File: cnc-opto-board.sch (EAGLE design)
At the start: 25 parts, among them J1 TTL, J2 FIELD, J3 POWER, Q1 P2N2222A, Q2 P2N2222A, U1 ATTINY85

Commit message: UPDATE: sized board outline to fit DIN rail mount frame and routed.
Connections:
- net +24V: now also J3-3.1; no longer J3-1.1
- net +5V: now also J3-1.1; no longer J3-2.1
- net GND: now also J3-2.1; no longer J3-3.1
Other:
- moved on the sheet: J1-1, J1-2, J1-3, J1-4, J1-5, J2-1, J2-2, J2-3, J2-4, J2-5, J2-6, J3-1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

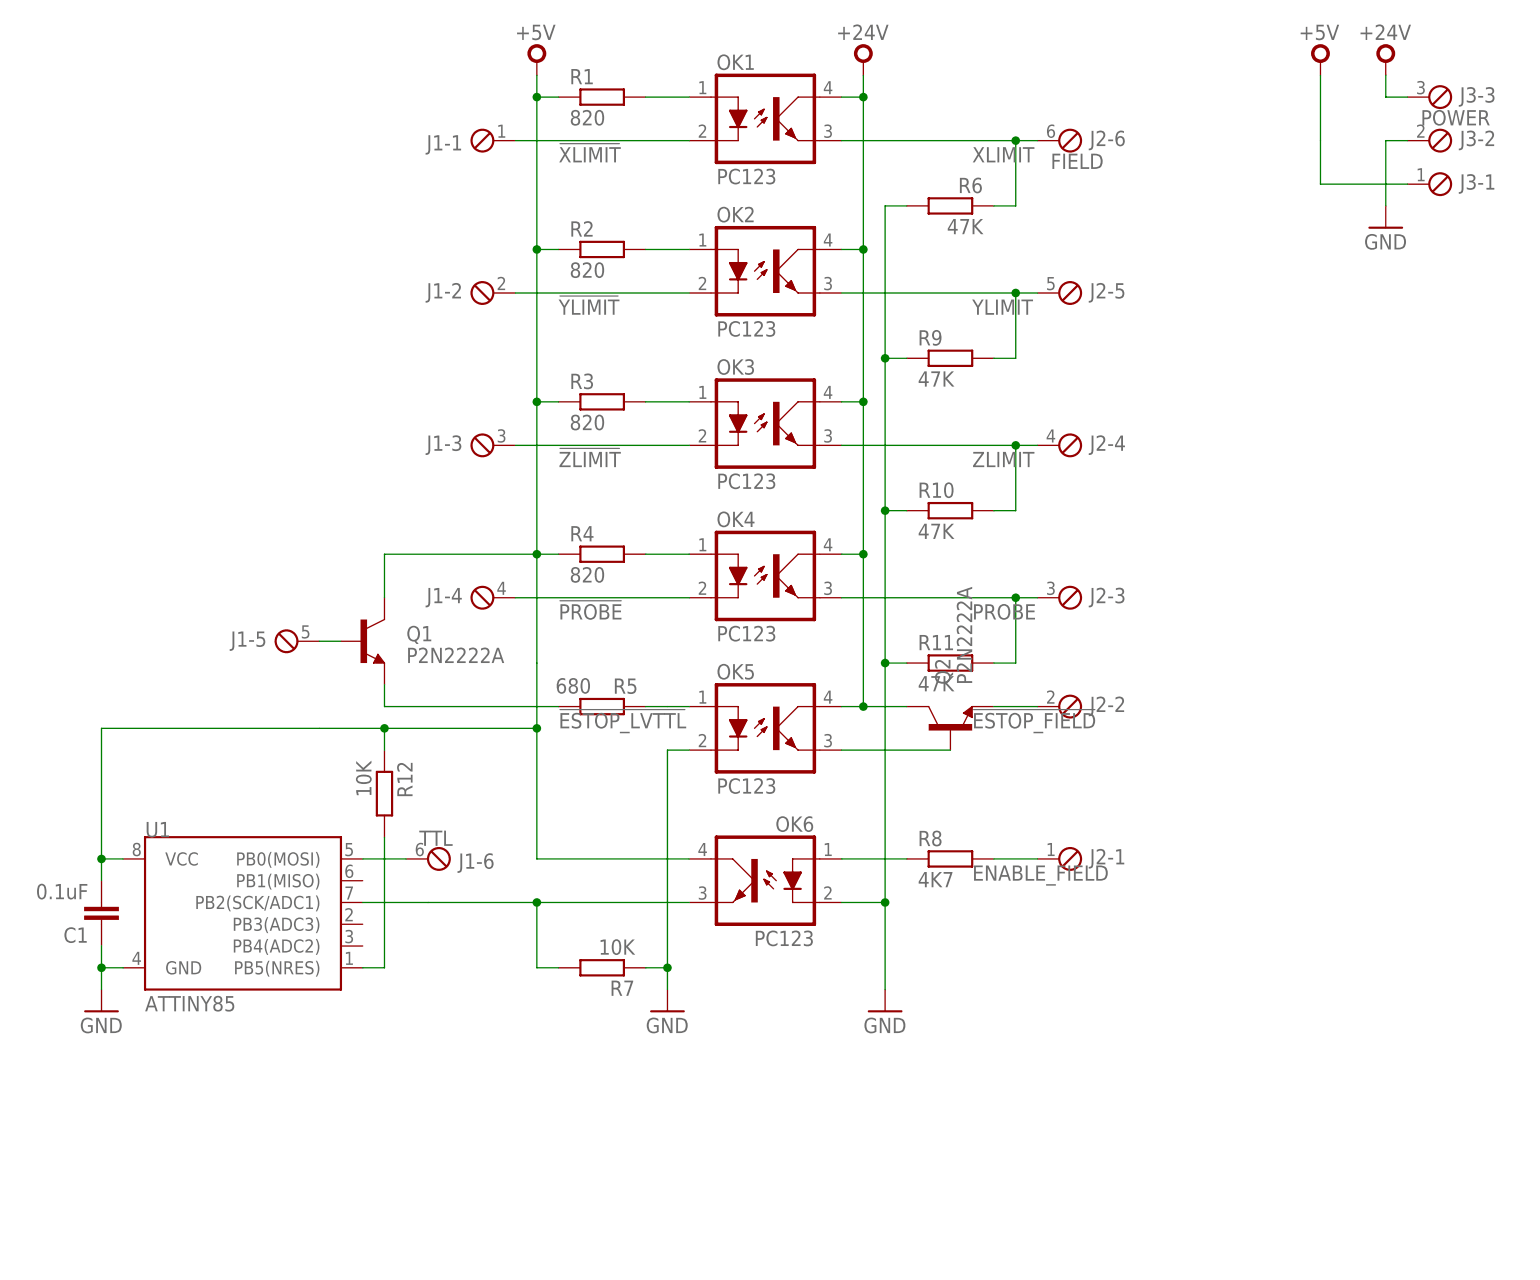
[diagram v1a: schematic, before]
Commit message: RTM: aesthetics and shrink-wrap for the opto board, ready for tape-out.
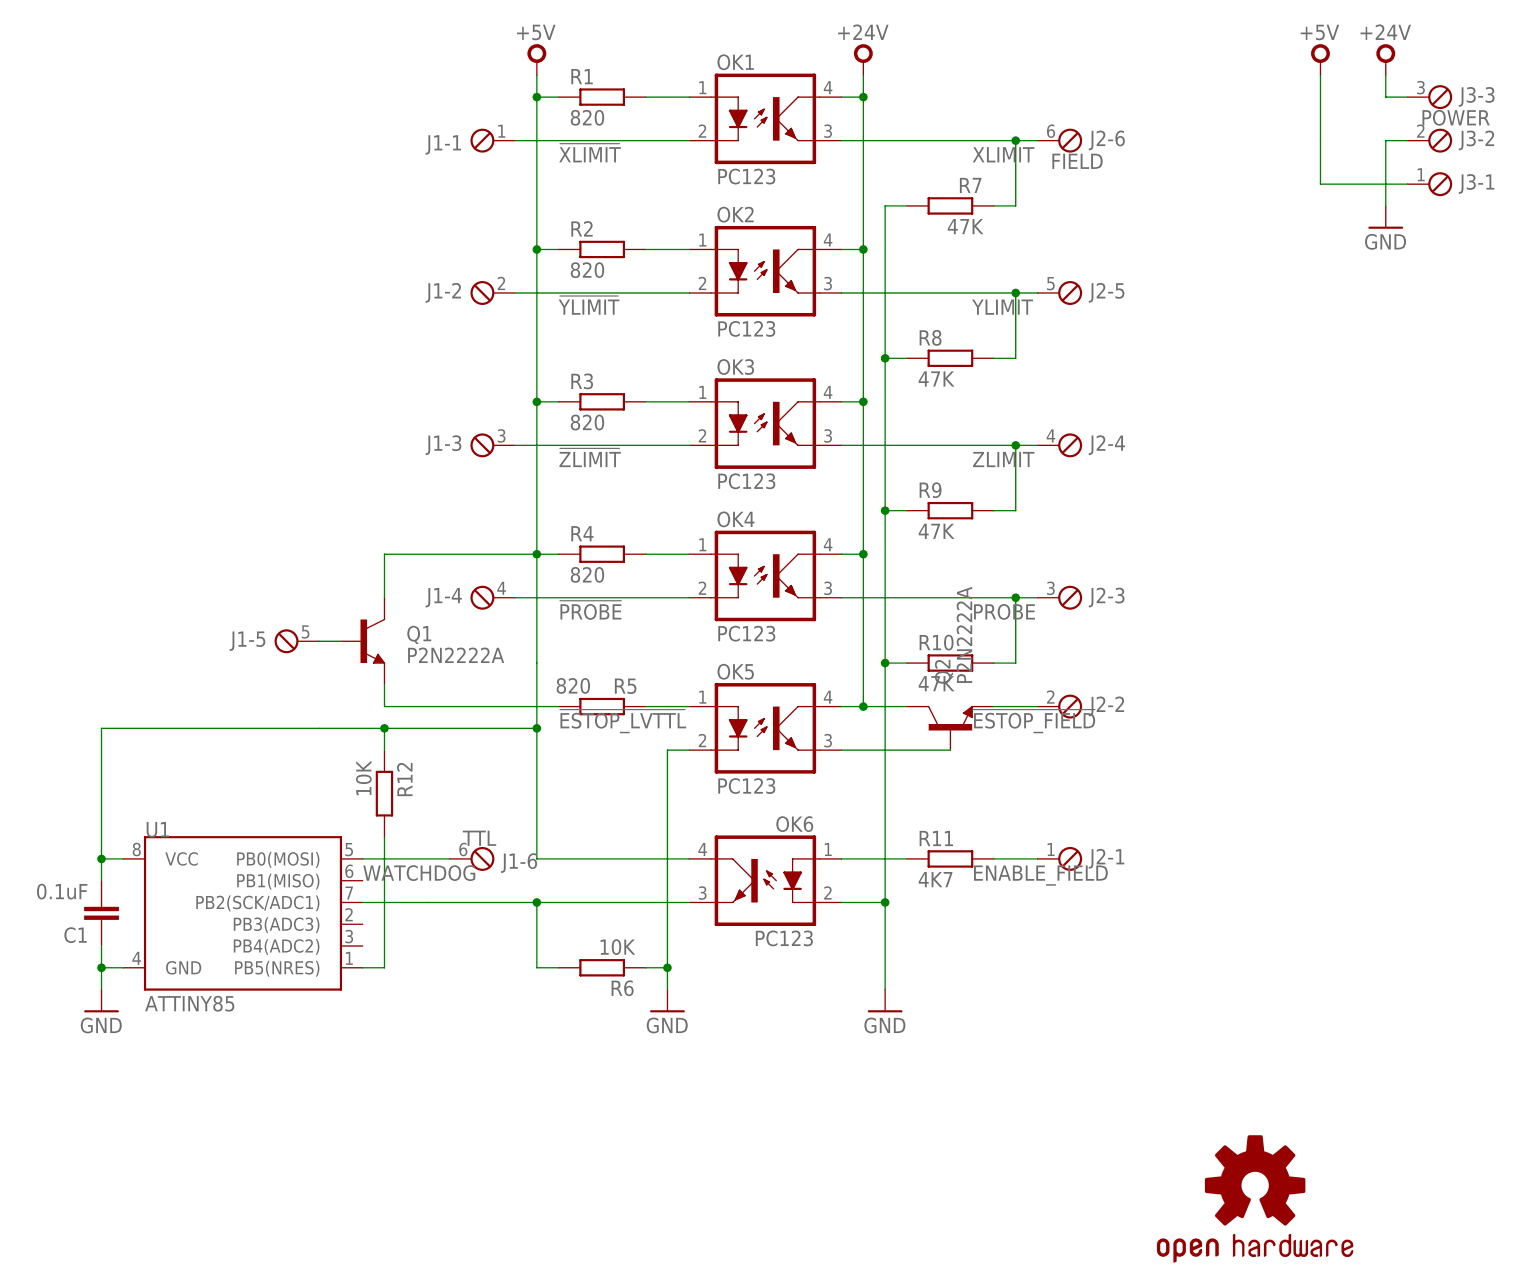
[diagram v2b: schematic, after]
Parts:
- added LOGO1: OSHW-LOGOL, SparkFun-Aesthetics:OSHW-LOGOL
- R11: value 47K -> 4K7
- R5: value 680 -> 820
- R6: value 47K -> 10K
- R7: value 10K -> 47K
- R8: value 4K7 -> 47K
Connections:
- net N$10 renamed WATCHDOG
- net ENABLE_FIELD: now also R11.2; no longer R8.2
- net ENABLE_TTL: now also R6.2; no longer R7.2
- net GND: now also R6.1, R7.2, R8.1; no longer R11.1, R6.2, R7.1
- net N$6: now also R11.1; no longer R8.1
- net PROBE: now also R10.2; no longer R11.2
- net XLIMIT: now also R7.1; no longer R6.1
- net YLIMIT: now also R8.2; no longer R9.2
- net ZLIMIT: now also R9.2; no longer R10.2
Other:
- moved on the sheet: J1-6, R10, R11, R6, R7, R8, R9
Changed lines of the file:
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@@
 <part name="R3" library="rcl" deviceset="R-EU_" device="0207/10" value="820"/>
 <part name="R4" library="rcl" deviceset="R-EU_" device="0207/10" value="820"/>
-<part name="R5" library="rcl" deviceset="R-EU_" device="0207/10" value="680"/>
+<part name="R5" library="rcl" deviceset="R-EU_" device="0207/10" value="820"/>
 <part name="V3" library="supply" deviceset="+24V" device=""/>
 <part name="V4" library="supply" deviceset="+5V" device=""/>
 <part name="GND2" library="supply1" deviceset="GND" device=""/>
-<part name="R7" library="rcl" deviceset="R-EU_" device="0207/10" value="10K"/>
+<part name="R6" library="rcl" deviceset="R-EU_" device="0207/10" value="10K"/>
 <part name="GND3" library="supply1" deviceset="GND" device=""/>
-<part name="R8" library="rcl" deviceset="R-EU_" device="0207/10" value="4K7"/>
-<part name="R6" library="rcl" deviceset="R-EU_" device="0207/10" value="47K"/>
+<part name="R11" library="rcl" deviceset="R-EU_" device="0207/10" value="4K7"/>
+<part name="R7" library="rcl" deviceset="R-EU_" device="0207/10" value="47K"/>
+<part name="R8" library="rcl" deviceset="R-EU_" device="0207/10" value="47K"/>
 <part name="R9" library="rcl" deviceset="R-EU_" device="0207/10" value="47K"/>
 <part name="R10" library="rcl" deviceset="R-EU_" device="0207/10" value="47K"/>
-<part name="R11" library="rcl" deviceset="R-EU_" device="0207/10" value="47K"/>
 <part name="Q1" library="SparkFun-DiscreteSemi" deviceset="TRANSISTOR_NPN_2" device="PTH" value="P2N2222A"/>
 <part name="Q2" library="SparkFun-DiscreteSemi" deviceset="TRANSISTOR_NPN_2" device="PTH" value="P2N2222A"/>
@@
 <part name="R12" library="rcl" deviceset="R-EU_" device="0207/10" value="10K"/>
 <part name="C1" library="rcl" deviceset="C-EU" device="050-025X075" value="0.1uF"/>
+<part name="LOGO1" library="SparkFun-Aesthetics" deviceset="OSHW-LOGO" device="L"/>
 </parts>
 <sheets>
@@
 <instance part="J1" gate="-4" x="86.36" y="83.82" rot="MR0"/>
 <instance part="J1" gate="-5" x="63.5" y="78.74" rot="MR0"/>
-<instance part="J1" gate="-6" x="78.74" y="53.34" rot="MR180"/>
+<instance part="J1" gate="-6" x="83.82" y="53.34" rot="MR180"/>
 <instance part="J2" gate="-1" x="152.4" y="53.34"/>
 <instance part="J2" gate="-2" x="152.4" y="71.12"/>
@@
 <instance part="V4" gate="1" x="182.88" y="147.32"/>
 <instance part="GND2" gate="1" x="190.5" y="127"/>
-<instance part="R7" gate="G$1" x="99.06" y="40.64" rot="R180"/>
+<instance part="R6" gate="G$1" x="99.06" y="40.64" rot="R180"/>
 <instance part="GND3" gate="1" x="132.08" y="35.56"/>
-<instance part="R8" gate="G$1" x="139.7" y="53.34"/>
-<instance part="R6" gate="G$1" x="139.7" y="129.54" rot="MR0"/>
-<instance part="R9" gate="G$1" x="139.7" y="111.76"/>
-<instance part="R10" gate="G$1" x="139.7" y="93.98"/>
-<instance part="R11" gate="G$1" x="139.7" y="76.2"/>
+<instance part="R11" gate="G$1" x="139.7" y="53.34"/>
+<instance part="R7" gate="G$1" x="139.7" y="129.54" rot="MR0"/>
+<instance part="R8" gate="G$1" x="139.7" y="111.76"/>
+<instance part="R9" gate="G$1" x="139.7" y="93.98"/>
+<instance part="R10" gate="G$1" x="139.7" y="76.2"/>
 <instance part="Q1" gate="G$1" x="71.12" y="78.74"/>
 <instance part="Q2" gate="G$1" x="139.7" y="68.58" rot="R90"/>
@@
 <instance part="R12" gate="G$1" x="73.66" y="60.96" rot="R270"/>
 <instance part="C1" gate="G$1" x="40.64" y="45.72" rot="R180"/>
+<instance part="LOGO1" gate="G$1" x="175.26" y="15.24"/>
 </instances>
 <busses>
@@
 <wire x1="106.68" y1="66.04" x2="106.68" y2="40.64" width="0.1524" layer="91"/>
 <wire x1="106.68" y1="40.64" x2="106.68" y2="38.1" width="0.1524" layer="91"/>
-<pinref part="R7" gate="G$1" pin="1"/>
+<pinref part="R6" gate="G$1" pin="1"/>
 <wire x1="104.14" y1="40.64" x2="106.68" y2="40.64" width="0.1524" layer="91"/>
 <junction x="106.68" y="40.64"/>
@@
 <wire x1="132.08" y1="38.1" x2="132.08" y2="48.26" width="0.1524" layer="91"/>
 <wire x1="132.08" y1="48.26" x2="127" y2="48.26" width="0.1524" layer="91"/>
-<pinref part="R6" gate="G$1" pin="2"/>
+<pinref part="R7" gate="G$1" pin="2"/>
 <wire x1="134.62" y1="129.54" x2="132.08" y2="129.54" width="0.1524" layer="91"/>
 <wire x1="132.08" y1="129.54" x2="132.08" y2="111.76" width="0.1524" layer="91"/>
@@
 <wire x1="132.08" y1="76.2" x2="132.08" y2="48.26" width="0.1524" layer="91"/>
 <junction x="132.08" y="48.26"/>
-<pinref part="R9" gate="G$1" pin="1"/>
+<pinref part="R8" gate="G$1" pin="1"/>
 <wire x1="134.62" y1="111.76" x2="132.08" y2="111.76" width="0.1524" layer="91"/>
 <junction x="132.08" y="111.76"/>
-<pinref part="R10" gate="G$1" pin="1"/>
+<pinref part="R9" gate="G$1" pin="1"/>
 <wire x1="134.62" y1="93.98" x2="132.08" y2="93.98" width="0.1524" layer="91"/>
 <junction x="132.08" y="93.98"/>
-<pinref part="R11" gate="G$1" pin="1"/>
+<pinref part="R10" gate="G$1" pin="1"/>
 <wire x1="134.62" y1="76.2" x2="132.08" y2="76.2" width="0.1524" layer="91"/>
 <junction x="132.08" y="76.2"/>
@@
 <pinref part="OK6" gate="A" pin="EMIT"/>
 <wire x1="109.22" y1="48.26" x2="91.44" y2="48.26" width="0.1524" layer="91"/>
-<pinref part="R7" gate="G$1" pin="2"/>
+<pinref part="R6" gate="G$1" pin="2"/>
 <wire x1="93.98" y1="40.64" x2="91.44" y2="40.64" width="0.1524" layer="91"/>
 <wire x1="91.44" y1="40.64" x2="91.44" y2="48.26" width="0.1524" layer="91"/>
@@
 <net name="N$6" class="0">
 <segment>
-<pinref part="R8" gate="G$1" pin="1"/>
+<pinref part="R11" gate="G$1" pin="1"/>
 <pinref part="OK6" gate="A" pin="A"/>
 <wire x1="134.62" y1="53.34" x2="127" y2="53.34" width="0.1524" layer="91"/>
@@
 <net name="ENABLE_FIELD" class="0">
 <segment>
-<pinref part="R8" gate="G$1" pin="2"/>
+<pinref part="R11" gate="G$1" pin="2"/>
 <wire x1="144.78" y1="53.34" x2="149.86" y2="53.34" width="0.1524" layer="91"/>
 <label x="142.24" y="50.8" size="1.778" layer="95"/>
@@
 <label x="142.24" y="134.62" size="1.778" layer="95"/>
 <pinref part="J2" gate="-6" pin="1"/>
-<pinref part="R6" gate="G$1" pin="1"/>
+<pinref part="R7" gate="G$1" pin="1"/>
 <wire x1="147.32" y1="137.16" x2="127" y2="137.16" width="0.1524" layer="91"/>
 <wire x1="144.78" y1="129.54" x2="147.32" y2="129.54" width="0.1524" layer="91"/>
@@
 <label x="142.24" y="116.84" size="1.778" layer="95"/>
 <pinref part="J2" gate="-5" pin="1"/>
-<pinref part="R9" gate="G$1" pin="2"/>
+<pinref part="R8" gate="G$1" pin="2"/>
 <wire x1="147.32" y1="119.38" x2="127" y2="119.38" width="0.1524" layer="91"/>
 <wire x1="144.78" y1="111.76" x2="147.32" y2="111.76" width="0.1524" layer="91"/>
@@
 <label x="142.24" y="99.06" size="1.778" layer="95"/>
 <pinref part="J2" gate="-4" pin="1"/>
-<pinref part="R10" gate="G$1" pin="2"/>
+<pinref part="R9" gate="G$1" pin="2"/>
 <wire x1="147.32" y1="101.6" x2="127" y2="101.6" width="0.1524" layer="91"/>
 <wire x1="144.78" y1="93.98" x2="147.32" y2="93.98" width="0.1524" layer="91"/>
@@
 <wire x1="149.86" y1="83.82" x2="147.32" y2="83.82" width="0.1524" layer="91"/>
 <pinref part="J2" gate="-3" pin="1"/>
-<pinref part="R11" gate="G$1" pin="2"/>
+<pinref part="R10" gate="G$1" pin="2"/>
 <wire x1="147.32" y1="83.82" x2="127" y2="83.82" width="0.1524" layer="91"/>
 <wire x1="144.78" y1="76.2" x2="147.32" y2="76.2" width="0.1524" layer="91"/>
@@
 </segment>
 </net>
-<net name="N$10" class="0">
+<net name="WATCHDOG" class="0">
 <segment>
 <pinref part="U1" gate="G$1" pin="PB0(MOSI)"/>
-<wire x1="76.2" y1="53.34" x2="71.12" y2="53.34" width="0.1524" layer="91"/>
+<wire x1="81.28" y1="53.34" x2="71.12" y2="53.34" width="0.1524" layer="91"/>
 <pinref part="J1" gate="-6" pin="1"/>
-</segment>
-</net>
+<label x="71.12" y="50.8" size="1.778" layer="95"/>
+</segment>
+</net>
